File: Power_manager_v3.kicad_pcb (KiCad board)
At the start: 4 copper layers, 50 x 25 mm, 80 parts, among them J1 L_input, J2 Pow_mng_pow, J3 Load1, J4 Load2, J5 SWD (PLS5), J6 Dig_mod_iface, Q1 2N5551S, Q2 2N5551S, U1 DC12003, U2 G3MB-202PL, U3 G3MB-202PL, U4 DC5V_DC5V3V3_v3, U5 STM32F030F4Px, U6 HLW8112, U7 ADuM_I2C_v3, Y1 CSTCE8M, Y2 ABLS-3.579545MHZ-D-3-Y-T

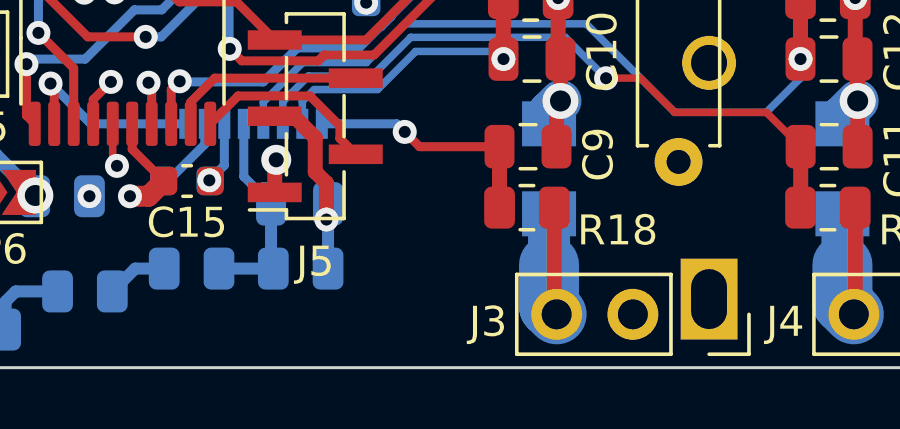
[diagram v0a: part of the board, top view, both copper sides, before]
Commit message: Сформирован перечень элементов, 3D-модель, исправлены ошибки, реализована панелизация платы.
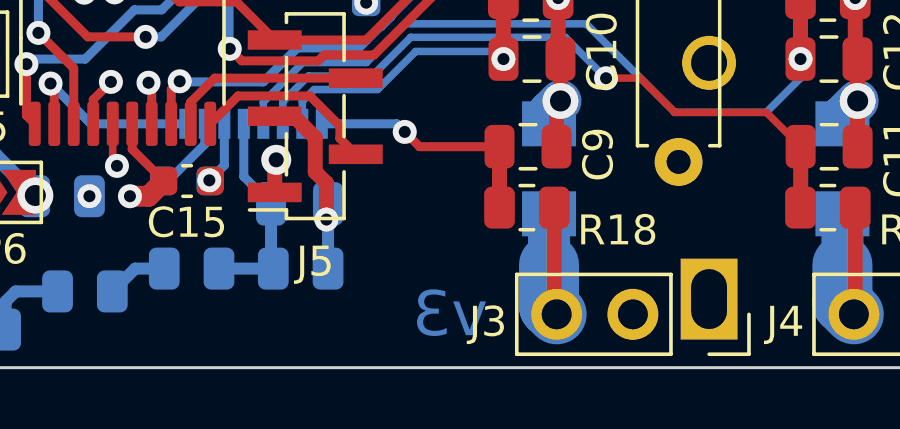
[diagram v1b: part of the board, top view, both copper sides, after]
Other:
- board text added: "v3"
